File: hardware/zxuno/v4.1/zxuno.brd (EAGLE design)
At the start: 86 x 56 mm, 103 parts, among them T1 BC846, U1 6SLX9TQG144, U2 FLASH-SPI-25XXSMD1, U4 AD724, U5 50MHz, U6 3.3V, U7 1.2V, Y1 3.58M, Y2 4.43M

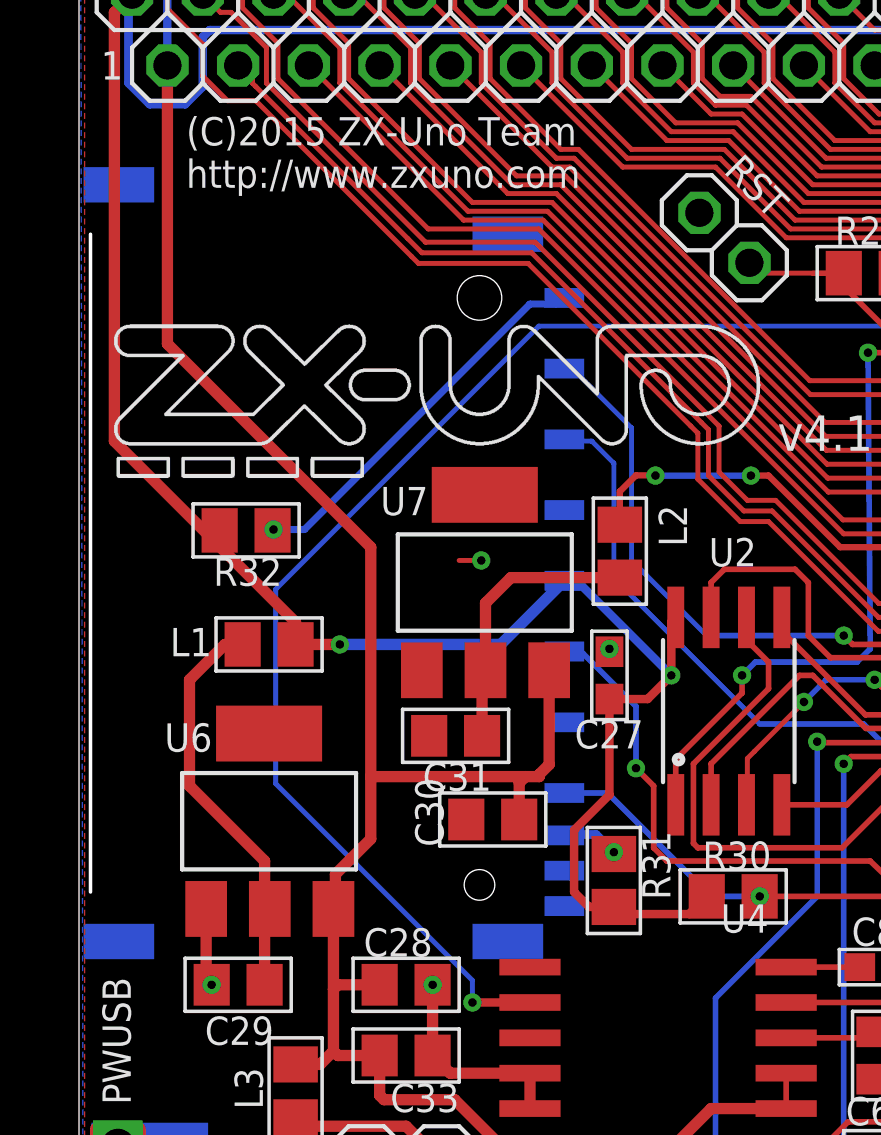
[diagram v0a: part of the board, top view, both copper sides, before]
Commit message: 5- Slot SD: Mover entre 1mm y 1.5mm hacia el lado del microUSB. Roza mucho con la carcasa puesta, mientras que el resto de conectores encajan bien
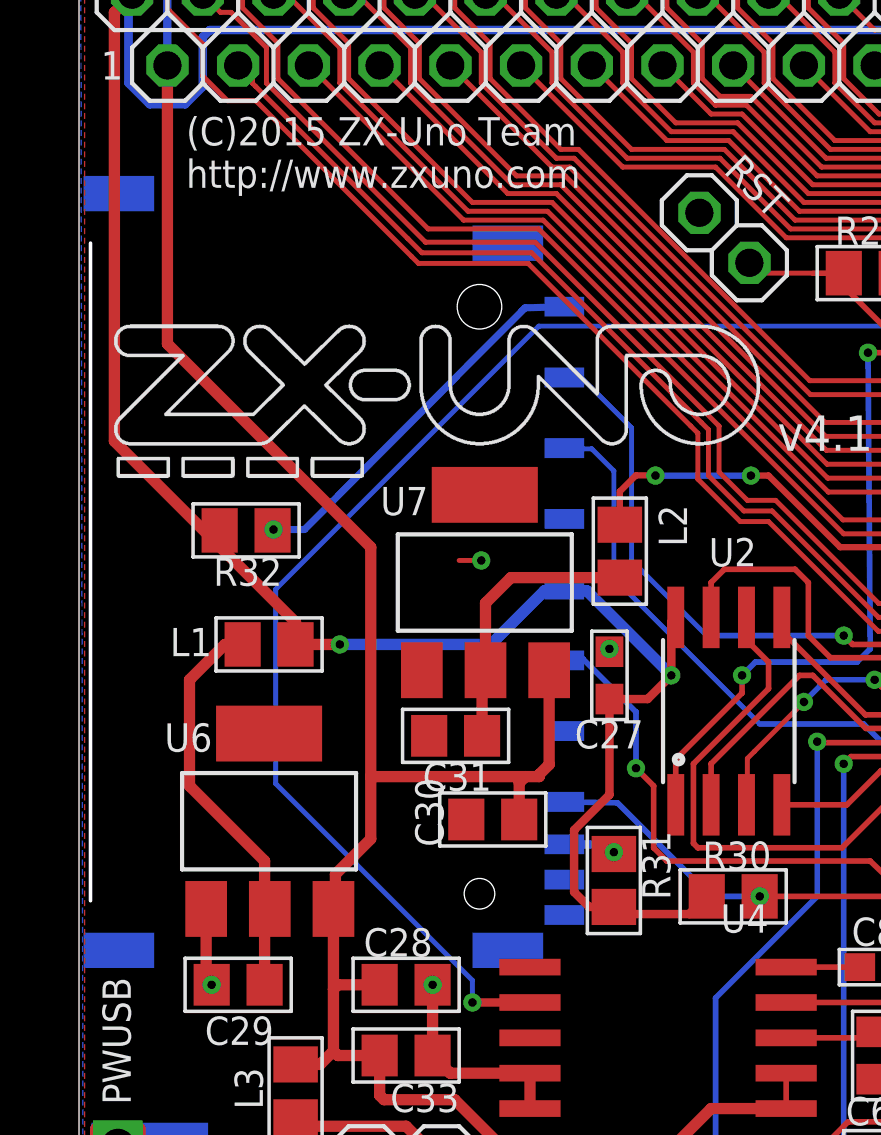
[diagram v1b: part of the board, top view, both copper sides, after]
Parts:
- moved SDCARD 0.32 mm to (3.97, 30.3)
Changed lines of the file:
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@@
 <attribute name="NAME" x="1.859509375" y="11.574090625" size="1.016" layer="25" font="vector" ratio="15" rot="SR90"/>
 </element>
-<element name="SDCARD" library="zxuno_rev_mcleod" package="SDCMF-10915W010" value="" x="3.96875" y="30.63875" smashed="yes" rot="MR90"/>
+<element name="SDCARD" library="zxuno_rev_mcleod" package="SDCMF-10915W010" value="" x="3.96875" y="30.32125" smashed="yes" rot="MR90"/>
 <element name="R31" library="rcl" package="M0805" value="10K" x="19.20875" y="19.6215" smashed="yes" rot="R270">
 <attribute name="NAME" x="20.22475" y="21.3995" size="1.016" layer="25" font="vector" ratio="15" rot="R270"/>
@@
 <wire x1="60.48375" y1="30.1625" x2="59.53125" y2="31.115" width="0.3048" layer="16"/>
 <wire x1="66.46625" y1="30.1125" x2="66.51625" y2="30.1625" width="0.3048" layer="16"/>
-<wire x1="9.36625" y1="28.09875" x2="15.14475" y2="28.09875" width="0.4064" layer="16"/>
+<wire x1="9.36625" y1="28.09875" x2="14.7875625" y2="28.09875" width="0.4064" layer="16"/>
 <wire x1="52.85125" y1="31.57125" x2="50.185" y2="31.57125" width="0.1778" layer="1"/>
 <wire x1="41.50125" y1="19.22125" x2="41.50125" y2="22.371875" width="0.3048" layer="1"/>
@@
 <via x="41.513125" y="22.38375" extent="1-16" drill="0.3048" diameter="0.6604"/>
 <wire x1="31.90875" y1="41.53296875" x2="31.80953125" y2="41.43375" width="0.4064" layer="16"/>
-<wire x1="17.87525" y1="30.38475" x2="21.2725" y2="26.9875" width="0.3048" layer="16"/>
 <via x="21.2725" y="26.9875" extent="1-16" drill="0.3048" diameter="0.6604"/>
 <wire x1="21.2725" y1="26.9875" x2="21.2725" y2="28.91155" width="0.3048" layer="1"/>
@@
 <wire x1="43.561" y1="2.06375" x2="43.581" y2="2.04375" width="0.2032" layer="1"/>
 <contactref element="SDCARD" pad="4"/>
-<wire x1="15.14475" y1="28.09875" x2="17.43075" y2="30.38475" width="0.4064" layer="16"/>
-<wire x1="17.87525" y1="30.38475" x2="17.43075" y2="30.38475" width="0.2032" layer="16"/>
 <contactref element="R31" pad="2"/>
 <contactref element="R32" pad="2"/>
@@
 <wire x1="66.46625" y1="30.1125" x2="66.46625" y2="22.83375" width="0.3048" layer="16"/>
 <wire x1="66.46625" y1="22.83375" x2="63.1325" y2="19.5" width="0.3048" layer="16"/>
+<wire x1="17.43075" y1="30.06725" x2="16.716375" y2="30.0275625" width="0.4064" layer="16"/>
+<wire x1="16.716375" y1="30.0275625" x2="14.7875625" y2="28.09875" width="0.4064" layer="16"/>
+<wire x1="17.43075" y1="30.06725" x2="18.2324375" y2="30.0275625" width="0.4064" layer="16"/>
+<wire x1="18.2324375" y1="30.0275625" x2="21.2725" y2="26.9875" width="0.4064" layer="16"/>
 <wire x1="51.038125" y1="34.44875" x2="51.038125" y2="34.471875" width="0" layer="19" extent="1-16"/>
 <wire x1="41.15265625" y1="39.608125" x2="41.17578125" y2="39.608125" width="0" layer="19" extent="1-16"/>
@@
 <wire x1="33.49625" y1="17.78" x2="33.49625" y2="19.21625" width="0.2032" layer="1"/>
 <wire x1="33.49625" y1="19.21625" x2="33.50125" y2="19.22125" width="0.2032" layer="1"/>
-<wire x1="18.415" y1="35.40125" x2="17.49425" y2="35.40125" width="0.1778" layer="16"/>
 <wire x1="31.27375" y1="18.7325" x2="32.7025" y2="17.30375" width="0.2032" layer="16"/>
 <wire x1="24.4475" y1="25.24125" x2="28.178125" y2="25.24125" width="0.2032" layer="16"/>
@@
 <wire x1="31.27375" y1="22.145625" x2="31.27375" y2="18.7325" width="0.2032" layer="16"/>
 <wire x1="24.4475" y1="25.24125" x2="19.20875" y2="30.48" width="0.1778" layer="16"/>
-<wire x1="19.20875" y1="30.48" x2="19.20875" y2="34.6075" width="0.1778" layer="16"/>
-<wire x1="19.20875" y1="34.6075" x2="18.415" y2="35.40125" width="0.1778" layer="16"/>
+<wire x1="19.20875" y1="30.48" x2="19.20875" y2="34.3296875" width="0.1778" layer="16"/>
+<wire x1="19.20875" y1="34.3296875" x2="18.415" y2="35.1234375" width="0.1778" layer="16"/>
 <contactref element="SDCARD" pad="2"/>
-<wire x1="17.49425" y1="35.40125" x2="17.43075" y2="35.46475" width="0.2032" layer="16"/>
+<wire x1="18.415" y1="35.1234375" x2="17.446625" y2="35.1234375" width="0.1778" layer="16"/>
+<wire x1="17.446625" y1="35.1234375" x2="17.43075" y2="35.14725" width="0.1778" layer="16"/>
 </signal>
 <signal name="SD_SCK">
@@
 <wire x1="34.00125" y1="17.3325" x2="33.17875" y2="16.51" width="0.2032" layer="1"/>
 <via x="20.0025" y="23.65375" extent="1-16" drill="0.3048" diameter="0.6604"/>
-<wire x1="20.0025" y1="23.65375" x2="20.0025" y2="25.87625" width="0.2032" layer="16"/>
+<wire x1="20.0025" y1="23.65375" x2="20.0025" y2="25.6778125" width="0.2032" layer="16"/>
 <wire x1="33.17875" y1="16.51" x2="32.385" y2="16.51" width="0.2032" layer="1"/>
 <wire x1="32.385" y1="16.51" x2="28.41625" y2="20.32" width="0.2032" layer="1"/>
 <wire x1="28.41625" y1="20.32" x2="21.11375" y2="20.32" width="0.2032" layer="1"/>
-<wire x1="18.0975" y1="27.78125" x2="17.49425" y2="27.78125" width="0.2032" layer="16"/>
-<wire x1="20.0025" y1="25.87625" x2="18.0975" y2="27.78125" width="0.2032" layer="16"/>
+<wire x1="20.0025" y1="25.6778125" x2="18.0975" y2="27.5828125" width="0.2032" layer="16"/>
 <contactref element="SDCARD" pad="5"/>
-<wire x1="17.49425" y1="27.78125" x2="17.43075" y2="27.84475" width="0.2032" layer="16"/>
 <wire x1="21.11375" y1="20.32" x2="20.6375" y2="20.79625" width="0.2032" layer="1"/>
 <wire x1="20.6375" y1="20.79625" x2="20.6375" y2="23.01875" width="0.2032" layer="1"/>
 <wire x1="20.6375" y1="23.01875" x2="20.0025" y2="23.65375" width="0.2032" layer="1"/>
+<wire x1="18.0975" y1="27.5828125" x2="17.526" y2="27.5828125" width="0.2032" layer="16"/>
+<wire x1="17.526" y1="27.5828125" x2="17.43075" y2="27.52725" width="0.2032" layer="16"/>
 </signal>
 <signal name="SD_MISO">
@@
 <wire x1="29.083" y1="19.05" x2="24.4475" y2="19.05" width="0.2032" layer="1"/>
 <contactref element="SDCARD" pad="7"/>
-<wire x1="17.43075" y1="22.76475" x2="18.9865" y2="22.76475" width="0.2032" layer="16"/>
-<wire x1="18.9865" y1="22.76475" x2="22.70125" y2="19.05" width="0.2032" layer="16"/>
+<wire x1="17.43075" y1="22.44725" x2="19.3436875" y2="22.4075625" width="0.2032" layer="16"/>
+<wire x1="19.3436875" y1="22.4075625" x2="22.70125" y2="19.05" width="0.2032" layer="16"/>
 <wire x1="22.70125" y1="19.05" x2="24.4475" y2="19.05" width="0.2032" layer="16"/>
 <wire x1="24.4475" y1="19.05" x2="24.445" y2="19.05" width="0" layer="19" extent="1-1"/>
@@
 <wire x1="27.78125" y1="28.09875" x2="27.46375" y2="28.41625" width="0.2032" layer="1"/>
 <contactref element="SDCARD" pad="1"/>
-<wire x1="17.43075" y1="38.00475" x2="17.653" y2="37.7825" width="0.2032" layer="16"/>
+<wire x1="17.43075" y1="37.68725" x2="17.653" y2="37.7825" width="0.2032" layer="16"/>
 </signal>
 <signal name="EXT7">
@@
 <via x="19.20875" y="20.6375" extent="1-16" drill="0.3048" diameter="0.6604"/>
 <wire x1="19.20875" y1="20.5715" x2="19.20875" y2="20.6375" width="0.3048" layer="1"/>
-<wire x1="19.20875" y1="20.6375" x2="18.57375" y2="21.2725" width="0.3048" layer="16"/>
-<wire x1="18.57375" y1="21.2725" x2="17.4625" y2="21.2725" width="0.3048" layer="16"/>
-<wire x1="17.4625" y1="21.2725" x2="17.43075" y2="21.24075" width="0.3048" layer="16"/>
+<wire x1="19.20875" y1="20.6375" x2="18.9309375" y2="20.9153125" width="0.3048" layer="16"/>
+<wire x1="18.9309375" y1="20.9153125" x2="17.8196875" y2="20.9153125" width="0.3048" layer="16"/>
+<wire x1="17.8196875" y1="20.9153125" x2="17.43075" y2="20.92325" width="0.3048" layer="16"/>
 </signal>
 <signal name="N$20">
 <contactref element="SDCARD" pad="9"/>
 <contactref element="R32" pad="1"/>
-<wire x1="17.43075" y1="40.54475" x2="17.36725" y2="40.54475" width="0.254" layer="16"/>
-<wire x1="17.36725" y1="40.54475" x2="17.145" y2="40.3225" width="0.254" layer="16"/>
-<wire x1="17.145" y1="40.3225" x2="16.1925" y2="40.3225" width="0.254" layer="16"/>
 <via x="6.985" y="32.22625" extent="1-16" drill="0.3048" diameter="0.6604"/>
 <wire x1="6.985" y1="32.22625" x2="7.07775" y2="32.0675" width="0.254" layer="1"/>
 <wire x1="7.07775" y1="32.0675" x2="6.95075" y2="32.1945" width="0.254" layer="1"/>
 <wire x1="6.985" y1="32.22625" x2="8.09625" y2="32.22625" width="0.254" layer="16"/>
-<wire x1="8.09625" y1="32.22625" x2="16.1925" y2="40.3225" width="0.254" layer="16"/>
+<wire x1="8.09625" y1="32.22625" x2="15.9146875" y2="40.084375" width="0.254" layer="16"/>
+<wire x1="17.43075" y1="40.22725" x2="16.017875" y2="40.1875625" width="0.254" layer="16"/>
+<wire x1="16.017875" y1="40.1875625" x2="15.9146875" y2="40.084375" width="0.254" layer="16"/>
 </signal>
 <signal name="N$15">

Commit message: 4- Las señales "R in" y "B in" del AD724 están intercambiadas y el color por video compuesto sale mal (por RGB sale bien). Corregir
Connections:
- net B: now also C8.2, R14.1, R18.1, R21.1, R3.1, RGB.7; no longer C6.2, R1.1, R12.1, R16.1, R19.1, RGB.5
- net B0: now also R21.2, U1.P88; no longer R19.2, U1.P79
- net B1: now also R18.2, U1.P92; no longer R16.2, U1.P80
- net B2: now also R14.2, U1.P93; no longer R12.2, U1.P81
- net R: now also C6.2, R1.1, R12.1, R16.1, R19.1, RGB.5; no longer C8.2, R14.1, R18.1, R21.1, R3.1, RGB.7
- net R0: now also R19.2, U1.P79; no longer R21.2, U1.P88
- net R1: now also R16.2, U1.P80; no longer R18.2, U1.P92
- net R2: now also R12.2, U1.P81; no longer R14.2, U1.P93
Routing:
- net R2: track 5.71 -> 9.97 mm
- net B2: track 9.97 -> 5.71 mm
- net R: track 30.4 -> 34.6 mm, vias 3 -> 2
- net B: track 34.6 -> 30.4 mm, vias 2 -> 3
- net R1: track 5.06 -> 7.51 mm
- net B1: track 7.51 -> 5.06 mm
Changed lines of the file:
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@@
 <wire x1="24.4475" y1="19.05" x2="24.445" y2="19.05" width="0" layer="19" extent="1-1"/>
 </signal>
-<signal name="B0">
+<signal name="R0">
 <contactref element="U1" pad="P79"/>
 <contactref element="R19" pad="2"/>
@@
 <wire x1="35.8775" y1="14.9225" x2="35.08125" y2="14.9225" width="0.2032" layer="1"/>
 </signal>
-<signal name="B1">
+<signal name="R1">
 <contactref element="U1" pad="P80"/>
 <contactref element="R16" pad="2"/>
@@
 <wire x1="36.03625" y1="12.85875" x2="35.08125" y2="12.85875" width="0.2032" layer="1"/>
 </signal>
-<signal name="B2">
+<signal name="R2">
 <contactref element="U1" pad="P81"/>
 <contactref element="R12" pad="2"/>
@@
 <wire x1="41.190365625" y1="3.767634375" x2="42.291" y2="2.667" width="0.1778" layer="1"/>
 </signal>
-<signal name="R0">
+<signal name="B0">
 <contactref element="U1" pad="P88"/>
 <contactref element="R21" pad="2"/>
@@
 <wire x1="40.50125" y1="14.5825" x2="40.64" y2="14.44375" width="0.2032" layer="1"/>
 </signal>
-<signal name="R1">
+<signal name="B1">
 <contactref element="U1" pad="P92"/>
 <contactref element="R18" pad="2"/>
@@
 <wire x1="43.18" y1="15.39875" x2="43.18" y2="14.44375" width="0.2032" layer="1"/>
 </signal>
-<signal name="R2">
+<signal name="B2">
 <contactref element="U1" pad="P93"/>
 <contactref element="R14" pad="2"/>
@@
 <wire x1="66.04" y1="8.66775" x2="65.96" y2="8.58775" width="0.2032" layer="1"/>
 </signal>
-<signal name="B">
+<signal name="R">
 <contactref element="R12" pad="1"/>
 <contactref element="R16" pad="1"/>
@@
 <wire x1="43.815" y1="10.31875" x2="43.8175" y2="10.31875" width="0" layer="19" extent="1-1"/>
 </signal>
-<signal name="R">
+<signal name="B">
 <contactref element="R14" pad="1"/>
 <contactref element="R18" pad="1"/>
